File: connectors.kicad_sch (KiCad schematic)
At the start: 7 parts, among them J2 Conn_01x02_Socket, J3 Conn_01x02_Socket, J4 Conn_01x02_Socket, Q2 DMP2305U

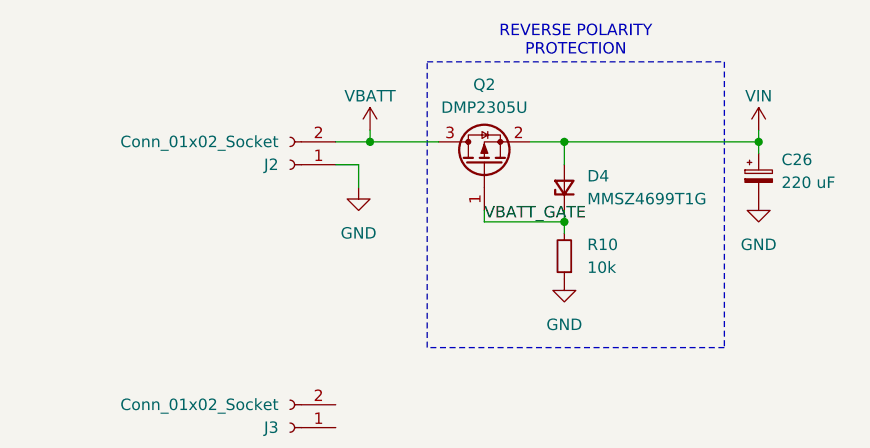
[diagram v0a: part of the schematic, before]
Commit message: Wired barometers and GPS up, added misc LEDs, tidy-up
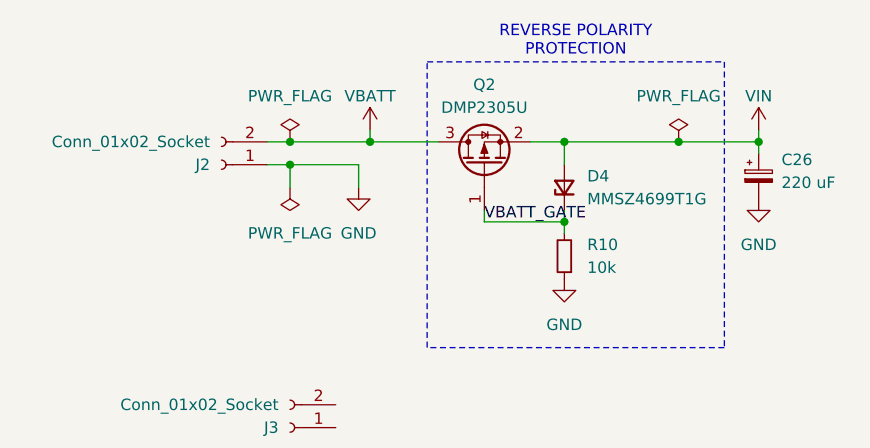
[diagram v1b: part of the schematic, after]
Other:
- moved on the sheet: J2

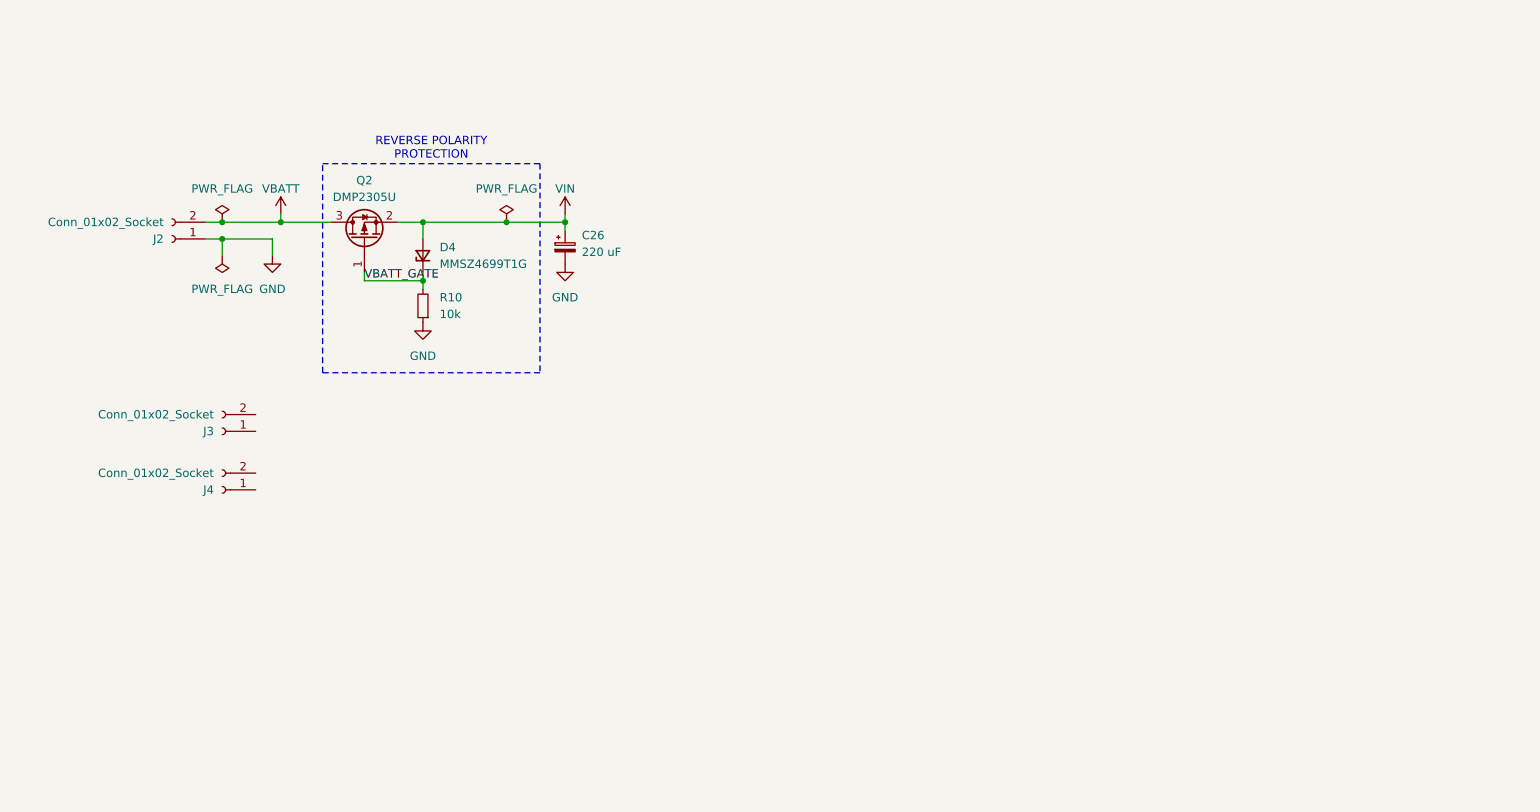
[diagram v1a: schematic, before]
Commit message: preliminary schematic wired, all footprints assigned, all laid out in PCB editor.
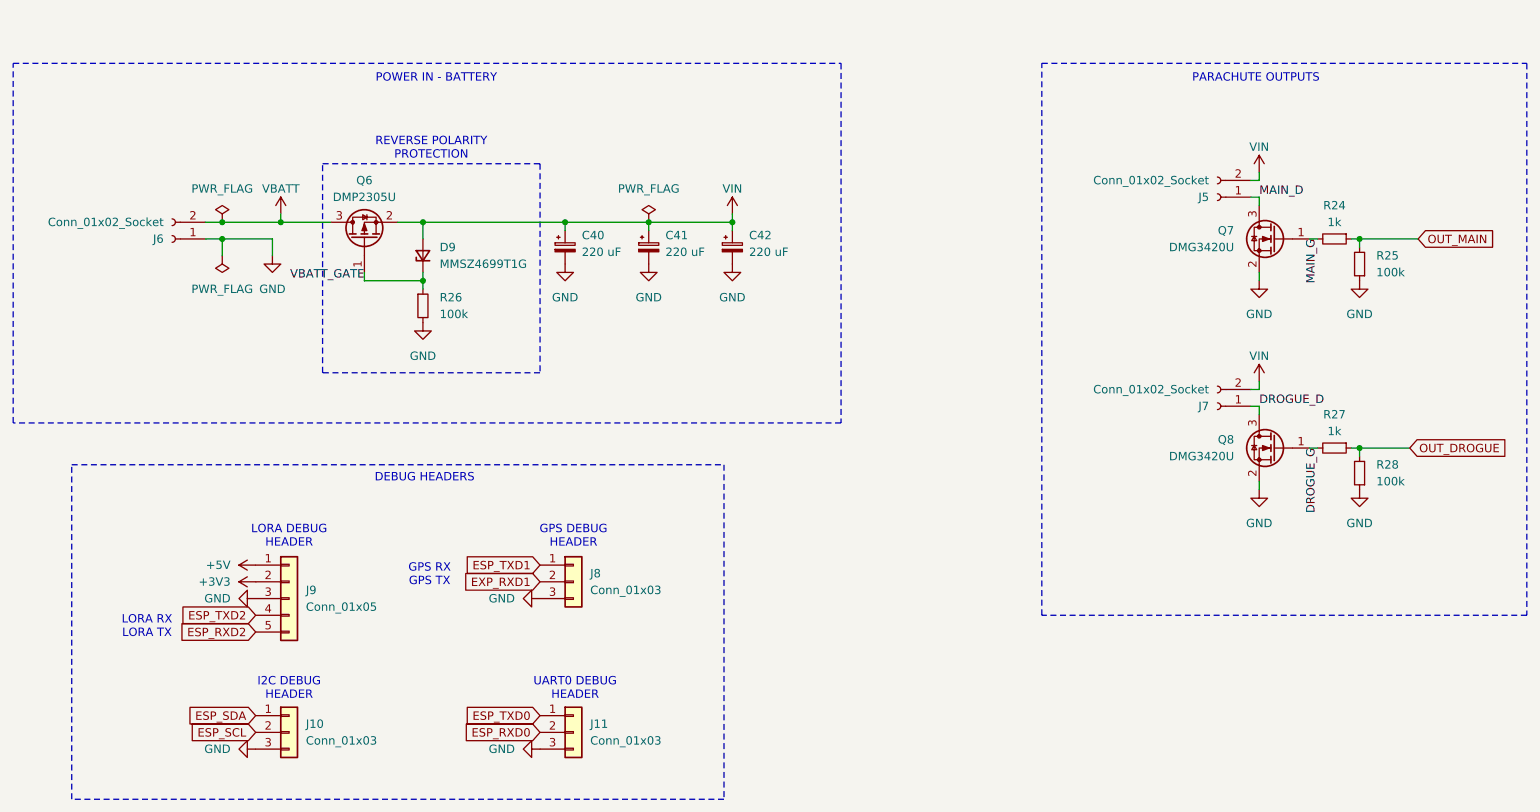
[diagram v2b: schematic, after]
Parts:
- removed R10: 10k, symbol Device:R_Small
- added C41, C42: 220 uF, Capacitor_SMD:CP_Elec_6.3x7.7, symbol Device:C_Polarized_Small
- added J10, J11, J8: Conn_01x03, Connector_PinHeader_2.54mm:PinHeader_1x03_P2.54mm_Vertical, symbol Connector_Generic:Conn_01x03
- added J9: Conn_01x05, Connector_PinHeader_2.54mm:PinHeader_1x05_P2.54mm_Vertical, symbol Connector_Generic:Conn_01x05
- added Q7, Q8: DMG3420U, Package_TO_SOT_SMD:SOT-23, symbol Transistor_FET:Q_NMOS_GSD
- added R24, R27: 1k, Resistor_SMD:R_0603_1608Metric, symbol Device:R_Small
- added R25, R26, R28: 100k, Resistor_SMD:R_0603_1608Metric, symbol Device:R_Small
- renumbered C26 to C40, D4 to D9, J3 to J5, J2 to J6, J4 to J7, Q2 to Q6
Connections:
- net GND: now also C41.2, C42.2, J10.3 (Pin_3), J11.3 (Pin_3), J8.3 (Pin_3), J9.3 (Pin_3), Q7.2 (S), Q8.2 (S), R25.1, R26.2, R28.1
- net VBATT_GATE: now also R26.1
- net VIN: now also J5.2 (Pin_2), J7.2 (Pin_2), C41.1, C42.1
- net DROGUE_D: now reaches J7.1 (Pin_1)
- net DROGUE_D: now also Q8.3 (D)
- net MAIN_D: now reaches J5.1 (Pin_1)
- net MAIN_D: now also Q7.3 (D)
- new net +3V3: J9.2 (Pin_2)
- new net +5V: J9.1 (Pin_1)
- new net DROGUE_G: Q8.1 (G), R27.2
- new net ESP_RXD0: J11.2 (Pin_2)
- new net ESP_RXD2: J9.5 (Pin_5)
- new net ESP_SCL: J10.2 (Pin_2)
- new net ESP_SDA: J10.1 (Pin_1)
- new net ESP_TXD0: J11.1 (Pin_1)
- new net ESP_TXD1: J8.1 (Pin_1)
- new net ESP_TXD2: J9.4 (Pin_4)
- new net EXP_RXD1: J8.2 (Pin_2)
- new net MAIN_G: Q7.1 (G), R24.2
- new net OUT_DROGUE: R27.1, R28.2
- new net OUT_MAIN: R24.1, R25.2
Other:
- note added: "DEBUG HEADERS"
- note added: "GPS DEBUG HEADER"
- note added: "GPS RX GPS TX"
- note added: "I2C DEBUG HEADER"
- note added: "LORA DEBUG HEADER"
- note added: "LORA RX LORA TX"
- note added: "PARACHUTE OUTPUTS"
- note added: "POWER IN - BATTERY"
- note added: "UART0 DEBUG HEADER"
- moved on the sheet: J5, J7

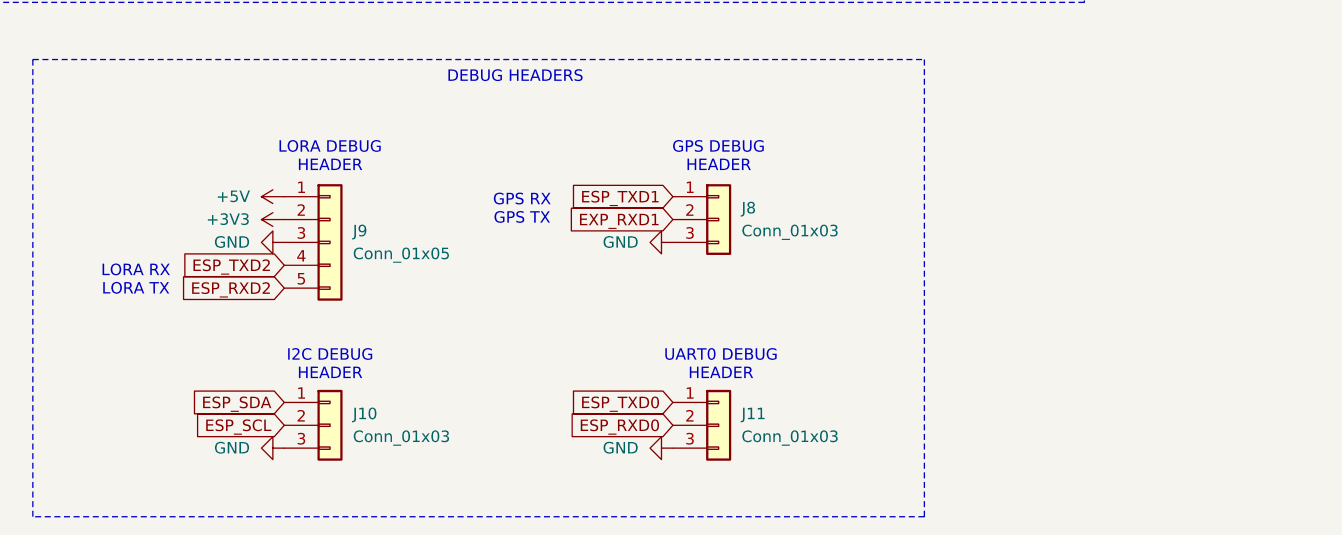
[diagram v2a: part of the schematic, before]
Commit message: reassigned some footprints, preliminary PCB layout
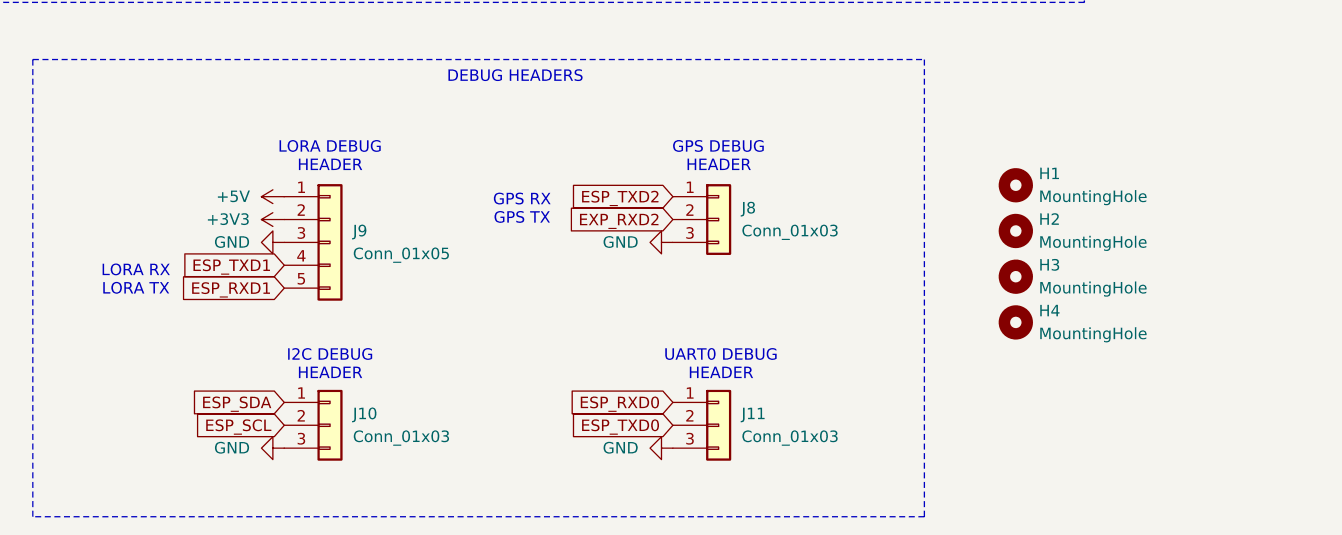
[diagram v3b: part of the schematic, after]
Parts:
- added H1, H2, H3, H4: MountingHole, symbol Mechanical:MountingHole
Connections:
- net ESP_RXD0: now also J11.1 (Pin_1); no longer J11.2 (Pin_2)
- net ESP_TXD0: now also J11.2 (Pin_2); no longer J11.1 (Pin_1)
- net ESP_TXD1: now also J9.4 (Pin_4); no longer J8.1 (Pin_1)
- net ESP_TXD2: now also J8.1 (Pin_1); no longer J9.4 (Pin_4)
- net ESP_RXD2 renamed ESP_RXD1
- net EXP_RXD1 renamed EXP_RXD2

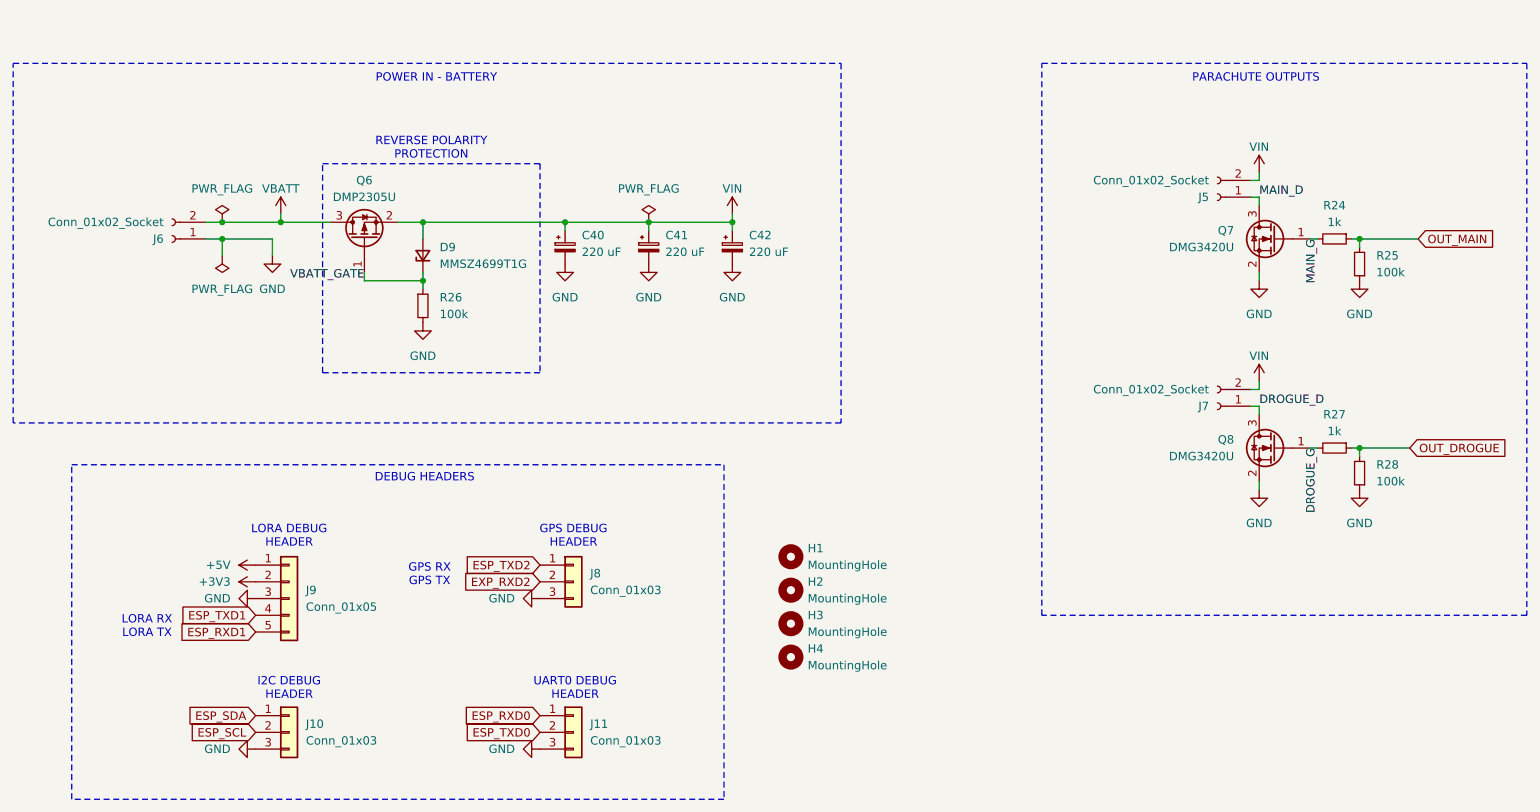
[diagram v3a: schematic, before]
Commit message: added missing output diodes, added 3d models, misc. re-laying
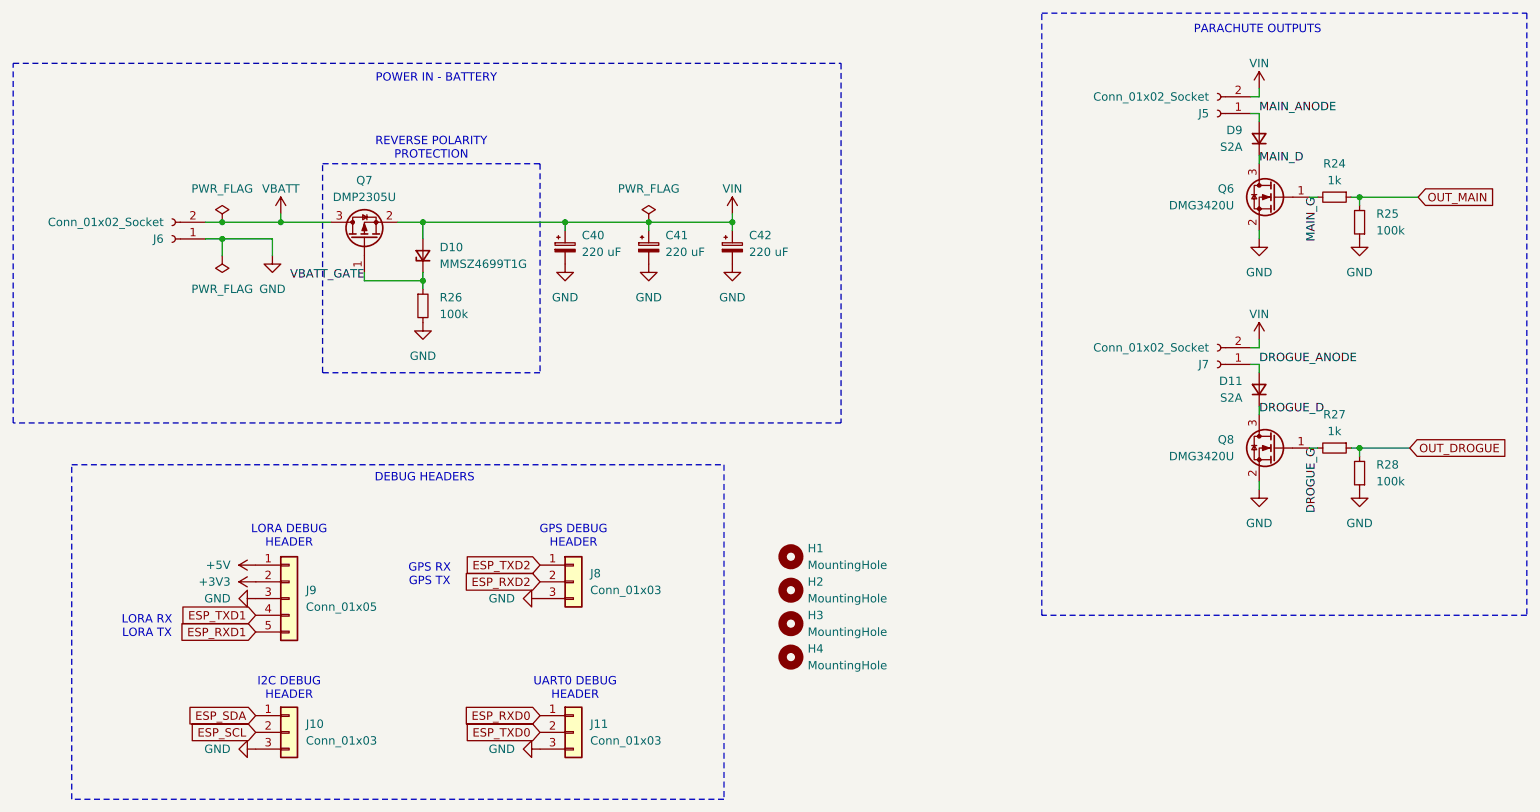
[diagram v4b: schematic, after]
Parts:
- added D11, D9: S2A, Diode_SMD:D_SMB, symbol Device:D_Small
- renumbered D9 to D10, Q7 to Q6, Q6 to Q7
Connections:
- net DROGUE_D: now also D11.1 (K); no longer J7.1 (Pin_1)
- net MAIN_D: now also D9.1 (K); no longer J5.1 (Pin_1)
- net EXP_RXD2 renamed ESP_RXD2
- new net DROGUE_ANODE: D11.2 (A), J7.1 (Pin_1)
- new net MAIN_ANODE: D9.2 (A), J5.1 (Pin_1)
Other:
- moved on the sheet: J5, J7, Q6, R24, R25

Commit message: revision of layout. added 3d model of the card
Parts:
- H1, H2, H3, H4: footprint (none) -> MountingHole:MountingHole_2.2mm_M2
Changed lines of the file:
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@@
 			)
 		)
-		(property "Footprint" ""
+		(property "Footprint" "MountingHole:MountingHole_2.2mm_M2"
 			(at 147.32 119.38 0)
 			(effects
@@
 			)
 		)
-		(property "Footprint" ""
+		(property "Footprint" "MountingHole:MountingHole_2.2mm_M2"
 			(at 147.32 124.46 0)
 			(effects
@@
 			)
 		)
-		(property "Footprint" ""
+		(property "Footprint" "MountingHole:MountingHole_2.2mm_M2"
 			(at 147.32 134.62 0)
 			(effects
@@
 			)
 		)
-		(property "Footprint" ""
+		(property "Footprint" "MountingHole:MountingHole_2.2mm_M2"
 			(at 147.32 129.54 0)
 			(effects

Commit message: did some clean-up, did some to-do tasks.
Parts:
- renumbered D9 to D10, D10 to D11, D11 to D12, Q8 to Q10, Q6 to Q8, Q7 to Q9, R24 to R28, R25 to R29, R26 to R30, R27 to R31, R28 to R32
